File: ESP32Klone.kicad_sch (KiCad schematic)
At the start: 23 parts, among them J1 USB_C_Receptacle_USB2.0_14P, J2 Conn_01x14_Socket, J3 Conn_01x14_Socket, U1 CH340G, U2 AMS1117-3.3, U3 ESP32-WROOM-32E, X1 12MHz

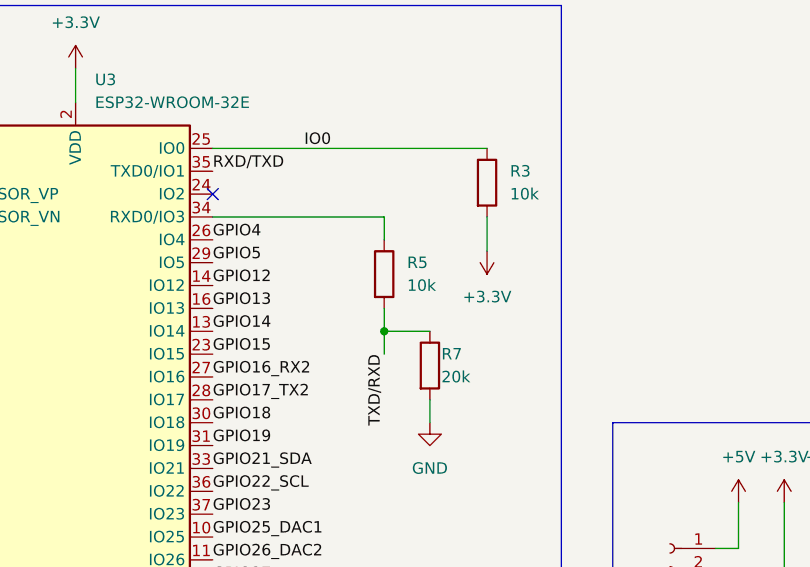
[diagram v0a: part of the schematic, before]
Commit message: fix: correct UART Rx level shifter wiring (R5/R7)
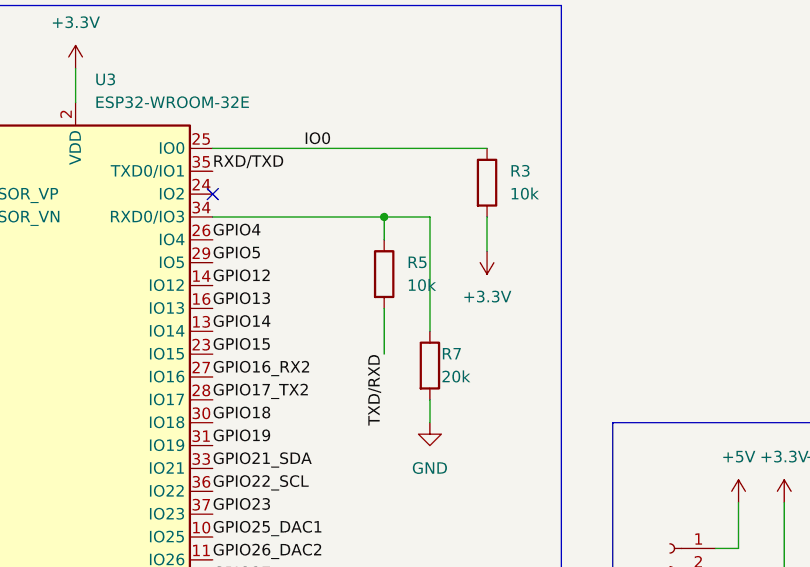
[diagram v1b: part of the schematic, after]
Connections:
- net TXD/RXD: no longer R7.1
- net at R5.1, U3.34 (RXD0/IO3): now also R7.1
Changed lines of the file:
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@@
-	)
-	(junction
-		(at 201.93 93.98)
-		(diameter 0)
-		(color 0 0 0 0)
 	)
 	(junction
@@
 	)
 	(junction
+		(at 201.93 81.28)
+		(diameter 0)
+		(color 0 0 0 0)
+	)
+	(junction
 		(at 157.48 44.45)
 		(diameter 0)
@@
 	(wire
 		(pts
-			(xy 201.93 91.44) (xy 201.93 93.98)
-		)
-		(stroke
-			(width 0)
-			(type default)
-		)
-	)
-	(wire
-		(pts
 			(xy 77.47 116.84) (xy 77.47 120.65)
 		)
@@
 	(wire
 		(pts
+			(xy 207.01 93.98) (xy 207.01 81.28)
+		)
+		(stroke
+			(width 0)
+			(type default)
+		)
+	)
+	(wire
+		(pts
 			(xy 133.35 73.66) (xy 152.4 73.66)
 		)
@@
 	(wire
 		(pts
+			(xy 207.01 81.28) (xy 201.93 81.28)
+		)
+		(stroke
+			(width 0)
+			(type default)
+		)
+	)
+	(wire
+		(pts
 			(xy 66.04 139.7) (xy 69.85 139.7)
 		)
@@
 	(wire
 		(pts
-			(xy 201.93 93.98) (xy 201.93 96.52)
+			(xy 201.93 91.44) (xy 201.93 96.52)
 		)
 		(stroke
@@
 		)
 		(stroke
-			(width 0)
-			(type default)
-		)
-	)
-	(wire
-		(pts
-			(xy 201.93 93.98) (xy 207.01 93.98)
-		)
-		(stroke
